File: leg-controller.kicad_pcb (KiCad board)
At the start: 2 copper layers, 92 parts, among them J1 Power, J10 Motor, J11 Rotary_Encoder, J12 UART, J14 ISP, J15 Motor_E, J16 Motor_D, J17 Motor_F, J2 I2C, J3 Conn_02x01, J4 Motor, J5 Rotary_Encoder, J6 Conn_02x01, J7 Motor, J8 Rotary_Encoder, J9 Conn_02x01, Q1 Q_NPN_BEC, Q3 Q_NPN_BEC, Q5 Q_NPN_BEC, SW1 Function, U1 LD1117S33TR_SOT223, U2 ATmega644P-20AU, U3 OPA333xxDCK, U4 OPA333xxDCK, U5 OPA333xxDCK, Y1 12MHz

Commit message: First draft of a pcb layout
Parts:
- added REF**: MountingHole_3.2mm_M3_Pad, MountingHole:MountingHole_3.2mm_M3_Pad, F.Cu at (93.1, 154.1)
- added REF**: MountingHole_3.2mm_M3_Pad, MountingHole:MountingHole_3.2mm_M3_Pad, F.Cu at (93.1, 110.4)
- added REF**: MountingHole_3.2mm_M3_Pad, MountingHole:MountingHole_3.2mm_M3_Pad, F.Cu at (165.0, 153.7)
- added REF**: MountingHole_3.2mm_M3_Pad, MountingHole:MountingHole_3.2mm_M3_Pad, F.Cu at (165.1, 110.2)
- moved J17 130.2 mm to (157.7, 154.2), turned to 270 degrees
- moved J15 125.6 mm to (142.7, 154.3), turned to 270 degrees
- moved J16 106.0 mm to (127.6, 154.1), turned to 270 degrees
- moved SW1 104.4 mm to (106.8, 144.9), turned to 180 degrees
- moved J10 100.9 mm to (166.1, 140.1)
- moved C11 98.0 mm to (125.2, 145.8), turned to 180 degrees
- moved D5 97.7 mm to (161.6, 147.8)
- moved C6 95.2 mm to (128.5, 145.8), turned to 180 degrees
- moved U2 89.5 mm to (123.3, 132.4), turned to 270 degrees
- moved J7 89.4 mm to (166.2, 129.0)
- moved D9 86.4 mm to (205.1, 130.3), turned to 270 degrees
- moved R23 84.5 mm to (159.4, 136.5), turned to 180 degrees
- moved R42 81.5 mm to (205.1, 133.7), turned to 90 degrees
- moved J6 77.9 mm to (157.9, 131.4), turned to 90 degrees
- moved R12 76.7 mm to (192.0, 124.2), turned to 180 degrees
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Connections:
- J11 pad 1: +8V -> +3V3
- J5 pad 1: +8V -> +3V3
- J8 pad 1: +8V -> +3V3
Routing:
- net GNDPWR: track 0.00 -> 1.56 mm, vias 0 -> 1
- added copper zone on B.Cu, net GND
- added copper zone on B.Cu, net GNDPWR

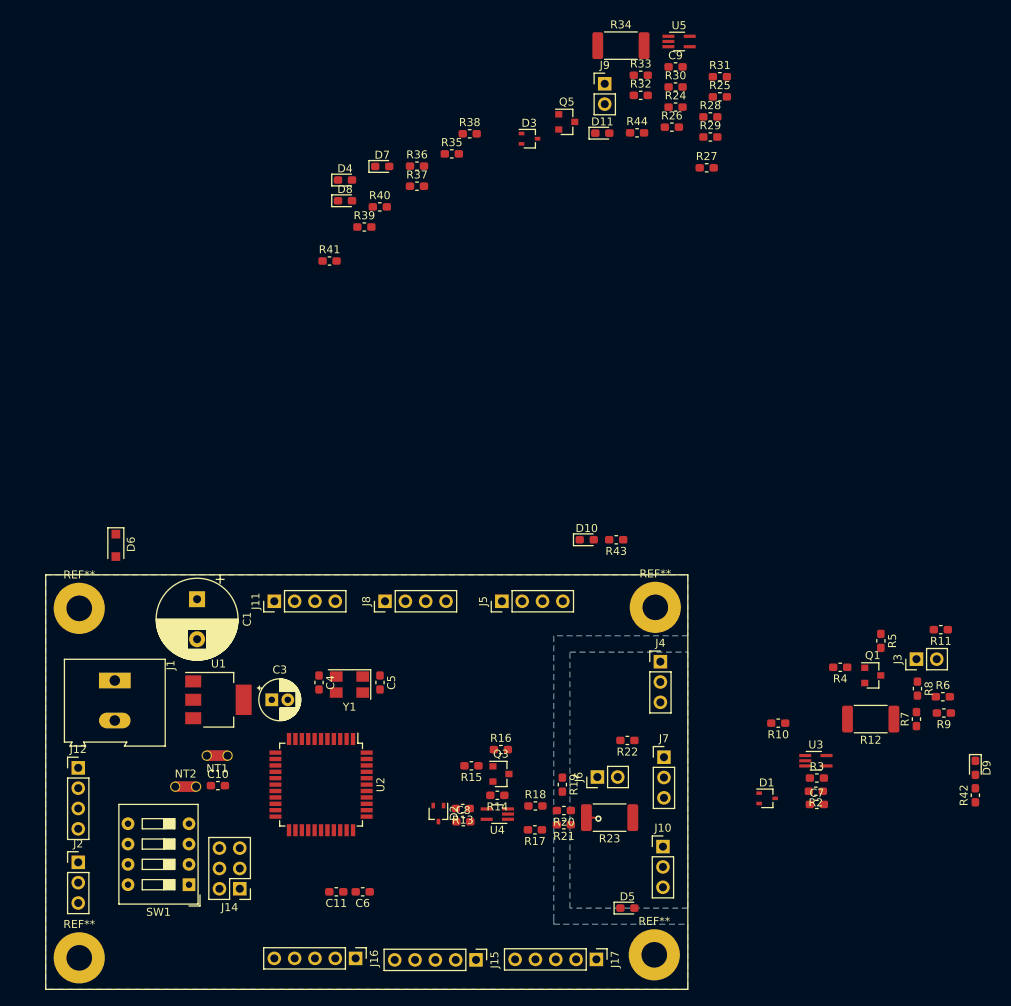
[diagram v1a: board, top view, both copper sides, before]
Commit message: Placed components on the PCB
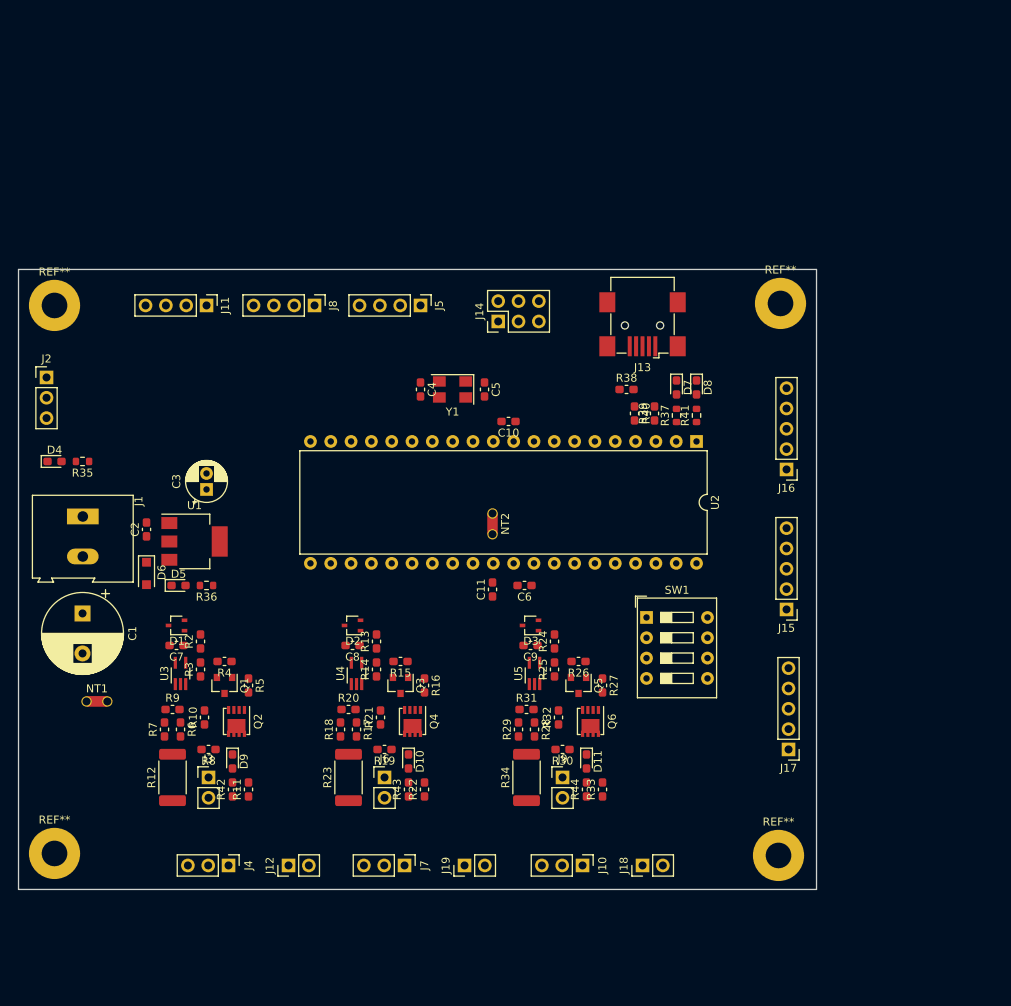
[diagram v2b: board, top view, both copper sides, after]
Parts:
- removed the REF** at (165.0, 153.7)
- removed the REF** at (165.1, 110.2)
- added C2: 100n, Capacitor_SMD:C_0603_1608Metric_Pad1.08x0.95mm_HandSolder, F.Cu at (101.5, 100.5)
- added J13: USB_B_Mini, Connector_USB:USB_Mini-B_Wuerth_65100516121_Horizontal, F.Cu at (163.5, 75.0)
- added J18: Conn_01x02, Connector_PinHeader_2.54mm:PinHeader_1x02_P2.54mm_Vertical, F.Cu at (163.5, 142.5)
- added J19: Conn_01x02, Connector_PinHeader_2.54mm:PinHeader_1x02_P2.54mm_Vertical, F.Cu at (141.2, 142.5)
- added Q2: SiSS05DN, Package_SO:Vishay_PowerPAK_1212-8_Single, F.Cu at (112.8, 124.5)
- added Q4: SiSS05DN, Package_SO:Vishay_PowerPAK_1212-8_Single, F.Cu at (134.8, 124.5)
- added Q6: SiSS05DN, Package_SO:Vishay_PowerPAK_1212-8_Single, F.Cu at (157.0, 124.5)
- added REF**: MountingHole_3.2mm_M3_Pad, MountingHole:MountingHole_3.2mm_M3_Pad, F.Cu at (180.5, 141.2)
- added REF**: MountingHole_3.2mm_M3_Pad, MountingHole:MountingHole_3.2mm_M3_Pad, F.Cu at (180.8, 72.2)
- J12: value UART -> Conn_01x02; footprint Connector_PinHeader_2.54mm:PinHeader_1x04_P2.54mm_Vertical -> Connector_PinHeader_2.54mm:PinHeader_1x02_P2.54mm_Vertical
- R35: value R -> 1.5k; footprint Resistor_SMD:R_0603_1608Metric_Pad1.05x0.95mm_HandSolder -> Resistor_SMD:R_0603_1608Metric
- R36, R37, R41: value R -> 330; footprint Resistor_SMD:R_0603_1608Metric_Pad1.05x0.95mm_HandSolder -> Resistor_SMD:R_0603_1608Metric
- R42, R43, R44: value R -> 1.5k
- U2: value ATmega644P-20AU -> ATmega644P-20PU; footprint Package_QFP:TQFP-44_10x10mm_P0.8mm -> Package_DIP:DIP-40_W15.24mm
- moved R9 96.4 mm to (104.8, 123.0), turned to 0 degrees
- moved R6 95.4 mm to (105.8, 125.5), turned to 270 degrees
- moved R7 94.0 mm to (103.8, 125.5)
- moved D9 92.9 mm to (112.2, 129.5)
- moved R42 92.9 mm to (112.2, 133.0)
- moved R34 92.2 mm to (149.0, 131.5), turned to 90 degrees
- moved J3 89.7 mm to (109.2, 131.5), turned to 0 degrees
- moved R33 89.4 mm to (158.5, 133.0), turned to 90 degrees
- moved R8 88.9 mm to (109.2, 128.0), turned to 180 degrees
- moved R11 88.8 mm to (114.2, 133.0), turned to 90 degrees
- moved R12 87.6 mm to (104.8, 131.5), turned to 90 degrees
- moved J9 86.9 mm to (153.5, 131.5)
- moved R30 84.0 mm to (153.5, 128.0), turned to 180 degrees
- moved R31 82.7 mm to (149.0, 123.0)
- moved C7 82.5 mm to (105.2, 115.0), turned to 180 degrees
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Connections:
- J12 pad 1: +3V3 -> LIMIT_SWITCH_A
- J12 pad 2: UART_TXD -> GND
- SW1 pad 3: FUNCTION_2 -> Net-(SW1-Pad3)
- SW1 pad 4: Net-(SW1-Pad4) -> RESET
- U2 pad 1: SPI_MOSI -> LED_RUN
- U2 pad 10: ROT_DAT_B -> +3V3
- U2 pad 11: UART_RXD -> GND
- U2 pad 12: UART_TXD -> Net-(C5-Pad1)
- U2 pad 13: SPI_SS_E -> Net-(C4-Pad1)
- U2 pad 14: SPI_SS_F -> ROT_CLK_B
- U2 pad 15: MOTOR_B_CONTROL -> ROT_DAT_B
- U2 pad 16: MOTOR_C_CONTROL -> LIMIT_SWITCH_B
- U2 pad 17: +3V3 -> LIMIT_SWITCH_C
- U2 pad 18: GND -> SPI_SS_E
- U2 pad 19: I2C_SCL -> SPI_SS_F
- U2 pad 2: SPI_MISO -> LED_ERR
- U2 pad 20: I2C_SDA -> MOTOR_B_CONTROL
- U2 pad 21: MOTOR_A_DISCONNECT -> MOTOR_C_CONTROL
- U2 pad 22: MOTOR_B_DISCONNECT -> I2C_SCL
- U2 pad 23: MOTOR_C_DISCONNECT -> I2C_SDA
- U2 pad 24: SPI_SS_D -> MOTOR_A_DISCONNECT
- U2 pad 25: ROT_CLK_C -> MOTOR_B_DISCONNECT
- U2 pad 26: ROT_DAT_C -> MOTOR_C_DISCONNECT
- U2 pad 27: +3.3VA -> SPI_SS_D
- U2 pad 28: GND -> ROT_CLK_C
- U2 pad 29: Net-(C6-Pad1) -> ROT_DAT_C
- U2 pad 3: SPI_SCK -> USB_D+
- U2 pad 30: ROT_DAT_A -> +3.3VA
- U2 pad 31: ROT_CLK_A -> GND
- U2 pad 32: FUNCTION_2 -> Net-(C6-Pad1)
- U2 pad 33: FUNCTION_1 -> ROT_DAT_A
- U2 pad 34: FUNCTION_0 -> ROT_CLK_A
- U2 pad 35: MOTOR_C_SENSE -> LIMIT_SWITCH_A
- U2 pad 36: MOTOR_B_SENSE -> FUNCTION_1
- U2 pad 37: MOTOR_A_SENSE -> FUNCTION_0
- U2 pad 38: +3V3 -> MOTOR_C_SENSE
- U2 pad 39: GND -> MOTOR_B_SENSE
- U2 pad 4: RESET -> USB_D-
- U2 pad 40: LED_RUN -> MOTOR_A_SENSE
- U2 pad 5: +3V3 -> MOTOR_A_CONTROL
- U2 pad 6: GND -> SPI_MOSI
- U2 pad 7: Net-(C5-Pad1) -> SPI_MISO
- U2 pad 8: Net-(C4-Pad1) -> SPI_SCK
- U2 pad 9: ROT_CLK_B -> RESET
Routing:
- net GNDPWR: track 1.56 -> 0.00 mm, vias 1 -> 0
- removed copper zone on B.Cu, net GND
- removed copper zone on B.Cu, net GNDPWR
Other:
- board outline added: 99.8 x 77.5 mm

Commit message: First draft of the leg controller PCB
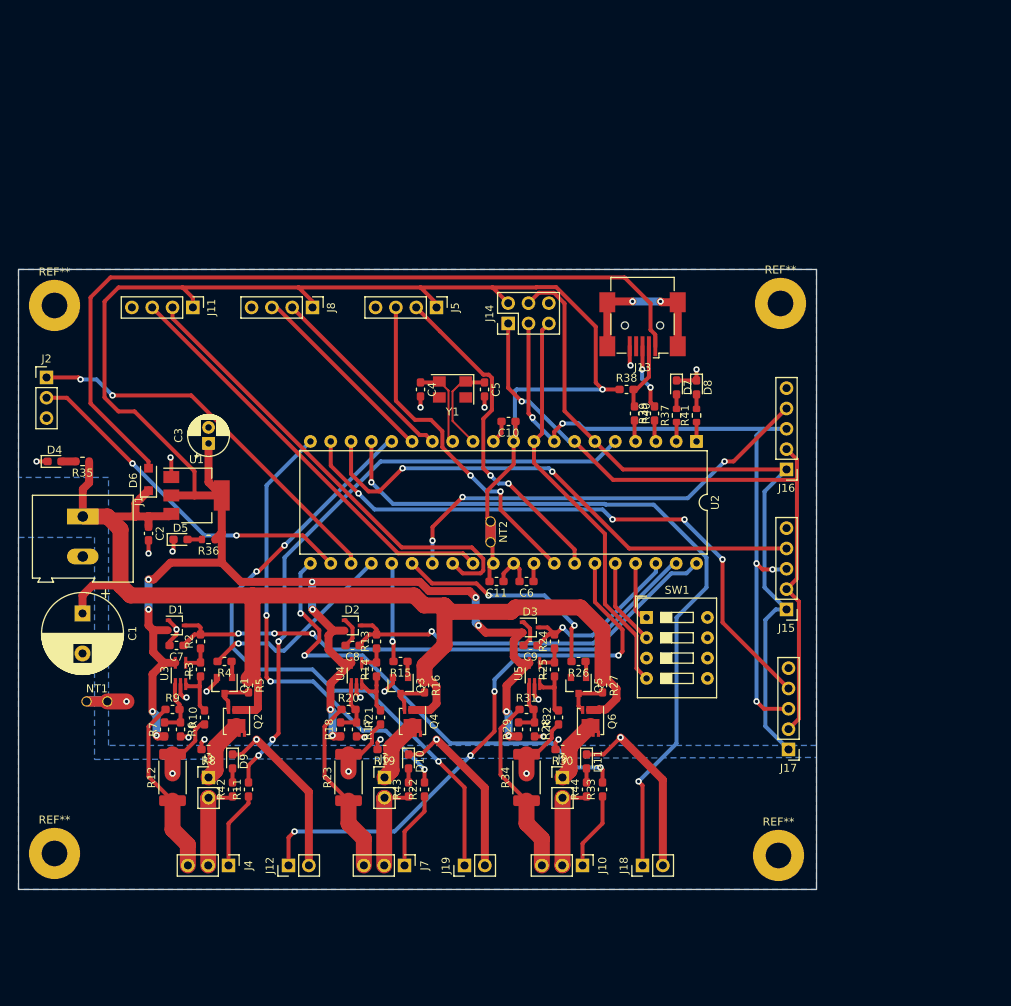
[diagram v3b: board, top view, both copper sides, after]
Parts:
- moved D6 11.8 mm to (101.8, 94.2), turned to 90 degrees
- moved C3 5.76 mm to (109.2, 89.8)
- moved D5 5.76 mm to (105.8, 101.8)
- moved R36 5.76 mm to (109.2, 101.8)
- moved U1 5.76 mm to (107.8, 96.2)
- moved J5 2.02 mm to (137.8, 72.8)
- moved J11 1.73 mm to (107.3, 72.8)
- moved J14 1.27 mm to (146.7, 74.8)
- moved C11 1.12 mm to (145.2, 107.0), turned to 180 degrees
- moved NT2 1.03 mm to (144.5, 99.5)
- moved C2 0.56 mm to (101.8, 101.0), turned to 270 degrees
- moved C6 0.56 mm to (149.0, 107.0)
- moved J8 0.35 mm to (122.2, 72.8)
- moved D3 0.25 mm to (149.5, 112.8), turned to 0 degrees
- turned D1 to 0 degrees
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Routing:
- net +3V3: track 0.00 -> 293.9 mm, vias 0 -> 13
- net +8V: track 0.00 -> 157.1 mm
- net GND: track 0.00 -> 125.3 mm, vias 0 -> 24
- net +5V: track 0.00 -> 102.3 mm
- net LIMIT_SWITCH_C: track 0.00 -> 93.1 mm, vias 0 -> 2
- net SPI_MOSI: track 0.00 -> 90.2 mm
- net SPI_SCK: track 0.00 -> 89.9 mm, vias 0 -> 5
- net SPI_MISO: track 0.00 -> 86.2 mm, vias 0 -> 1
- net LIMIT_SWITCH_B: track 0.00 -> 80.5 mm, vias 0 -> 3
- net MOTOR_A_CONTROL: track 0.00 -> 77.3 mm, vias 0 -> 3
- net SPI_SS_F: track 0.00 -> 76.5 mm, vias 0 -> 4
- net MOTOR_A_SENSE: track 0.00 -> 74.6 mm, vias 0 -> 3
- net LIMIT_SWITCH_A: track 0.00 -> 71.1 mm, vias 0 -> 4
- net SPI_SS_E: track 0.00 -> 64.8 mm, vias 0 -> 2
- net MOTOR_C_CONTROL: track 0.00 -> 58.7 mm, vias 0 -> 3
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- added copper zone on B.Cu, net GND
- added copper zone on B.Cu, net GNDPWR
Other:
- rule trace_min: 0.2 -> 0

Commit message: Reduced traces on back to make the ground planes denser
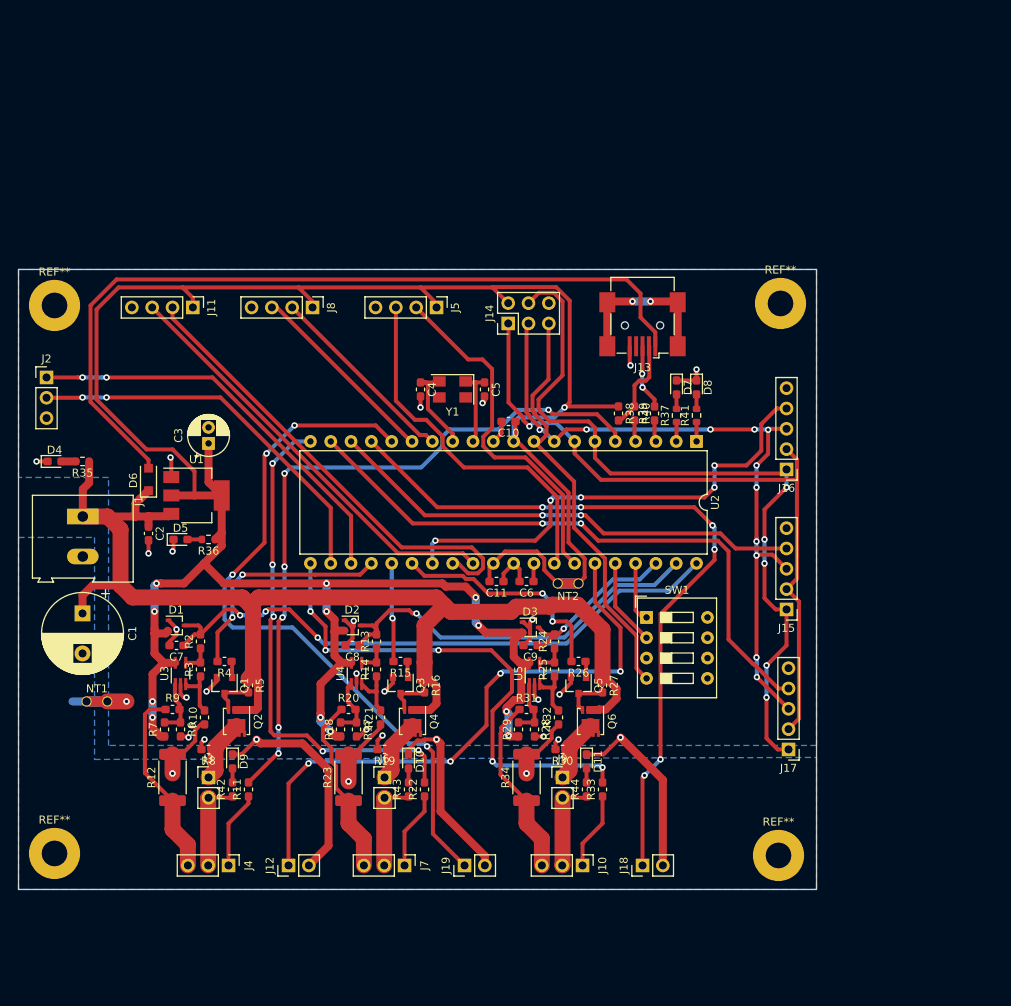
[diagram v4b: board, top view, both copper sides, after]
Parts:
- moved NT2 13.5 mm to (155.5, 107.2), turned to 180 degrees
- moved R38 3.16 mm to (160.5, 86.0), turned to 270 degrees
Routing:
- net MOTOR_A_CONTROL: track 77.3 -> 88.2 mm, vias 3 -> 6
- net GND: track 125.3 -> 135.8 mm, vias 24 -> 27
- net LIMIT_SWITCH_B: track 80.5 -> 90.0 mm, vias 3 -> 4
- net +3V3: track 293.9 -> 301.9 mm
- net SPI_MOSI: track 90.2 -> 97.8 mm, vias 0 -> 5
- net +3.3VA: track 6.14 -> 13.6 mm
- net MOTOR_B_CONTROL: track 57.9 -> 63.5 mm, vias 3 -> 5
- net MOTOR_C_CONTROL: track 58.7 -> 64.3 mm, vias 3 -> 5
- net SPI_SS_E: track 64.8 -> 60.0 mm
- net SPI_SS_D: track 55.1 -> 59.2 mm, vias 3 -> 5
- net I2C_SCL: track 44.1 -> 48.2 mm
- net LIMIT_SWITCH_A: track 71.1 -> 75.2 mm
- net MOTOR_A_DISCONNECT: track 25.1 -> 28.8 mm, vias 1 -> 2
- net ROT_DAT_A: track 42.4 -> 46.0 mm, vias 2 -> 0
- net Net-(J13-Pad2): track 8.59 -> 11.5 mm
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
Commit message: Fixed silkscreen labels
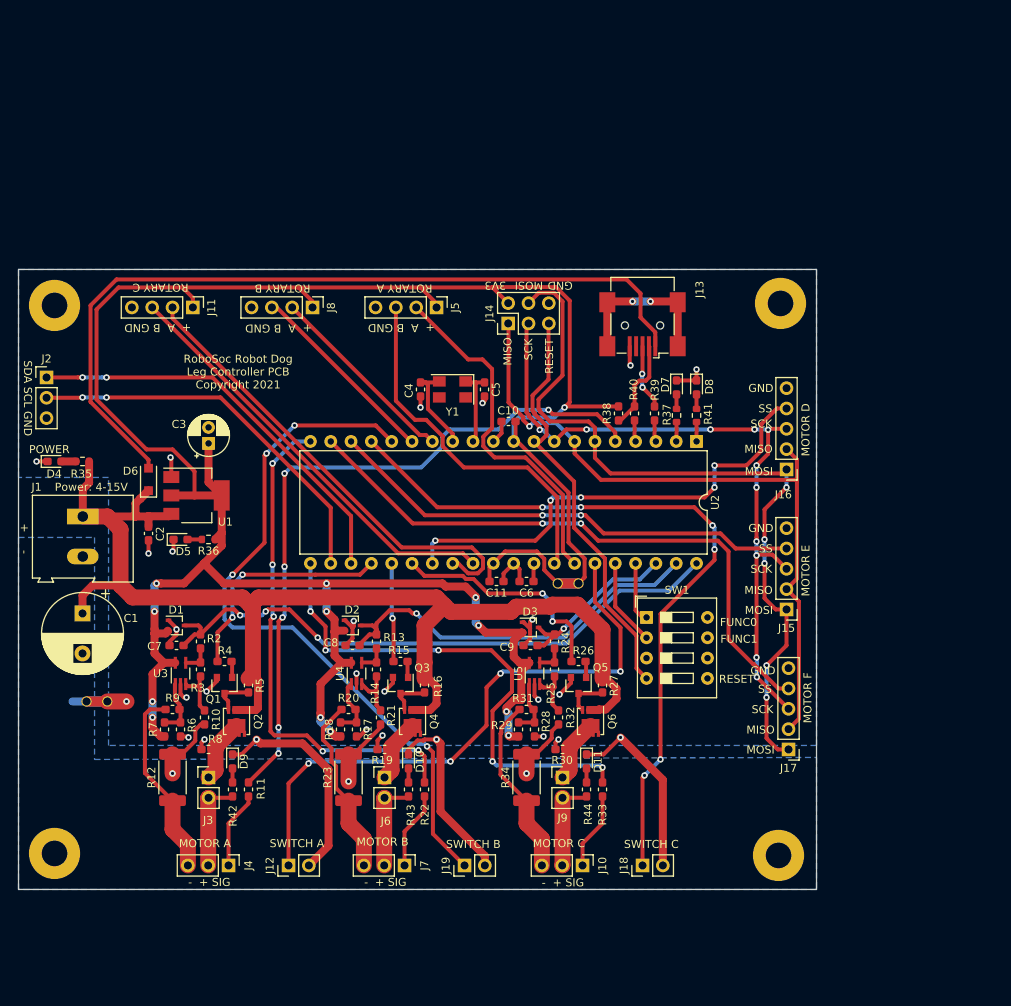
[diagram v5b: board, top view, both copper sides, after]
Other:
- board text added: "+ -"
- board text added: "+ A B GND"
- board text added: "- + SIG"
- board text added: "3V3"
- board text added: "FUNC0"
- board text added: "FUNC1"
- board text added: "GND"
- board text added: "MISO"
- board text added: "MOSI"
- board text added: "MOTOR A"
- board text added: "MOTOR B"
- board text added: "MOTOR C"
- board text added: "MOTOR D"
- board text added: "MOTOR E"
- board text added: "MOTOR F"
- board text added: "POWER"
- board text added: "Power: 4-15V"
- board text added: "RESET"
- board text added: "ROTARY A"
- board text added: "ROTARY B"
- board text added: "ROTARY C"
- board text added: "RoboSoc Robot Dog Leg Controller PCB Copyright 2021"
- board text added: "SCK"
- board text added: "SDA SCL GND"
- board text added: "SS"
- board text added: "SWITCH A"
- board text added: "SWITCH B"
- board text added: "SWITCH C"
